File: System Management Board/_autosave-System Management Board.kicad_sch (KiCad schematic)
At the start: 138 parts, among them IC1 SI2318CDS-T1-GE3, IC2 SI2318CDS-T1-GE3, IC3 SI2318CDS-T1-GE3, IC4 SI2318CDS-T1-GE3, IC5 SI2318CDS-T1-GE3, IC6 SI2318CDS-T1-GE3, J1 Conn_01x04_Male, J10 Conn_01x02_Male, J11 Conn_02x20_Odd_Even, J12 Conn_02x05_Top_Bottom, J13 Conn_01x04_Female, J2 Conn_01x04_Male, J3 Conn_01x02_Male, J4 PJ-063BH, J5 Conn_01x02_Male, J6 Conn_02x06_Counter_Clockwise, J7 Conn_02x20_Odd_Even, J8 Conn_01x02_Male, J9 Conn_01x02_Male, K1 J115F11CH5VDCS61.5U, K2 J114FL1CS165VDC.41, K3 J114FL1CS165VDC.41, SW1 SW_Push, SW2 SW_Push, U1 SC0915, U4 R1560S501B-E2-FE, U5 74HC4051, U6 MCP9700T-ETT, U7 MCP9700T-ETT

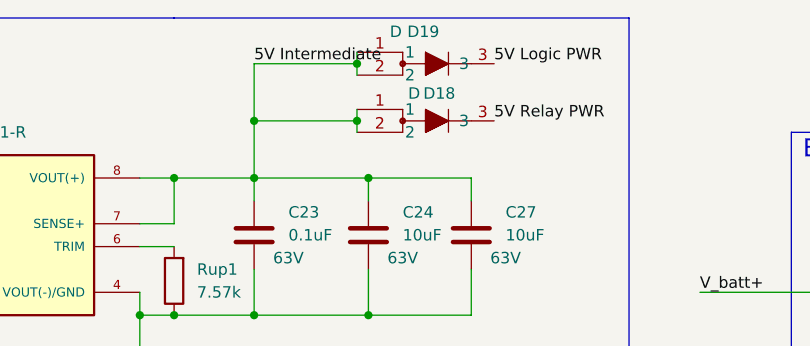
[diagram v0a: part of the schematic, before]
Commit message: minor changes naming or routing
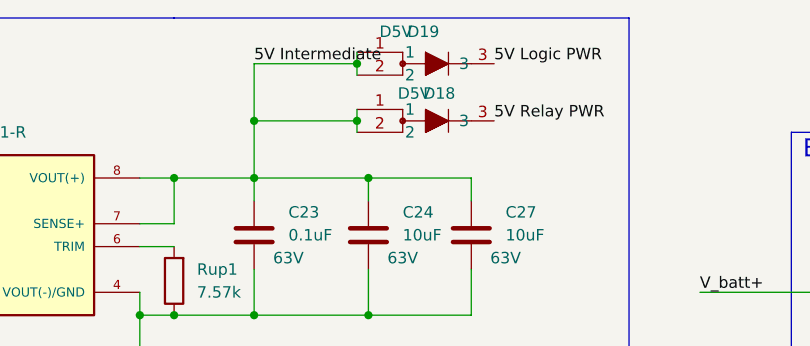
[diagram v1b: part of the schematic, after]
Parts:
- D18, D19: value D -> D5V
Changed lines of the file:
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@@
 			)
 		)
-		(property "Value" "D"
+		(property "Value" "D5V"
 			(at 326.898 16.764 0)
 			(effects
@@
 			)
 		)
-		(property "Value" "D"
+		(property "Value" "D5V"
 			(at 328.93 23.622 0)
 			(effects
